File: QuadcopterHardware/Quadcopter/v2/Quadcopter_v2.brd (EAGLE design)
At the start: 47 x 28 mm, 43 parts, among them J1 FTDI_DEVICE, M1 WIRELESS-NRF24L01, U1 ATMEGA328P_TQFP, U3 GY-521MPU6050

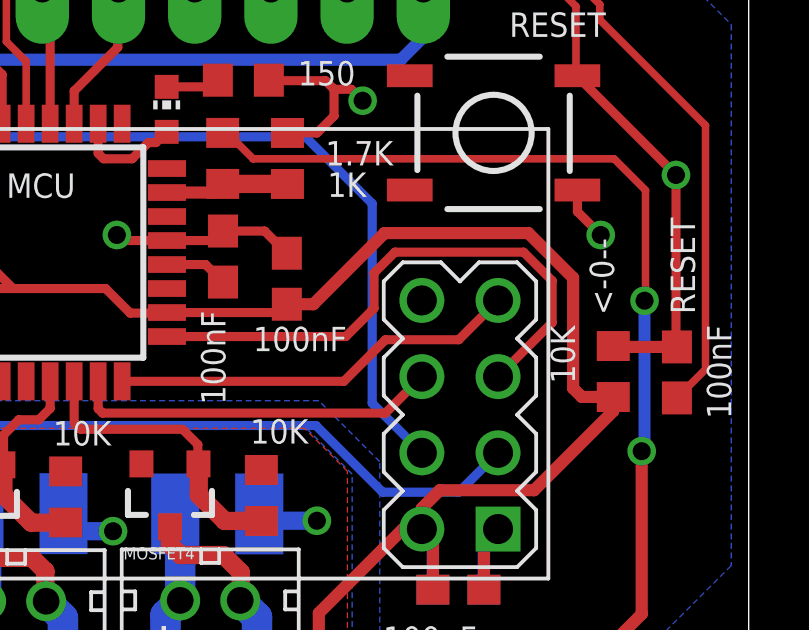
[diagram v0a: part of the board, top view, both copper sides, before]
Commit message: removed unnecessary trace
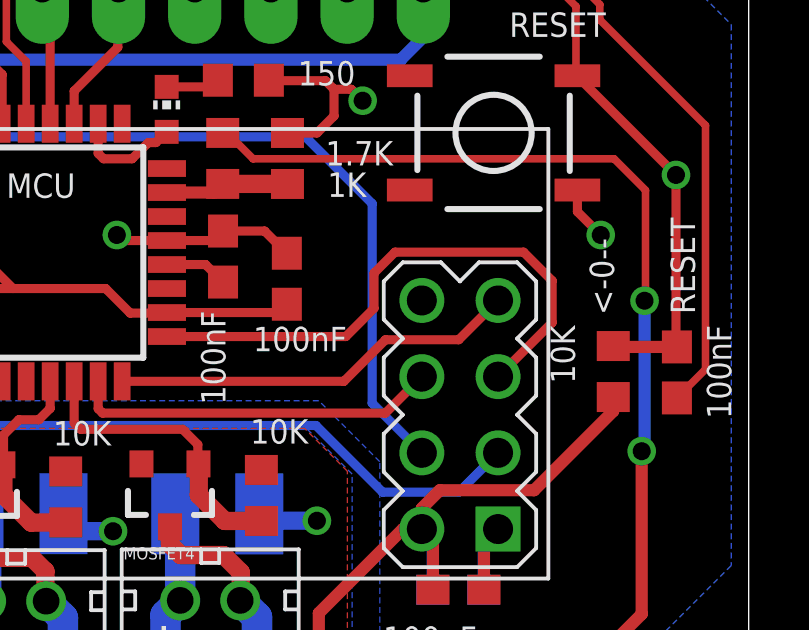
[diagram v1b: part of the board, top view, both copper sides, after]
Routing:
- net 3V3: track 146.4 -> 130.1 mm
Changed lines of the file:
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@@
 <wire x1="26.38425" y1="13.93825" x2="27.58985" y2="13.93825" width="0.3048" layer="1"/>
 <wire x1="27.58985" y1="13.93825" x2="27.60835" y2="13.95675" width="0.3048" layer="1"/>
-<wire x1="31.60575" y1="14.233" x2="32.48925" y2="14.233" width="0.4064" layer="1"/>
-<wire x1="32.48925" y1="14.233" x2="34.8615" y2="16.60525" width="0.4064" layer="1"/>
-<wire x1="34.8615" y1="16.60525" x2="39.65575" y2="16.60525" width="0.4064" layer="1"/>
-<wire x1="39.65575" y1="16.60525" x2="41.148" y2="15.113" width="0.4064" layer="1"/>
-<wire x1="41.148" y1="15.113" x2="41.148" y2="11.43" width="0.4064" layer="1"/>
-<wire x1="41.148" y1="11.43" x2="41.43375" y2="11.14425" width="0.4064" layer="1"/>
-<wire x1="41.43375" y1="11.14425" x2="42.482" y2="11.14425" width="0.4064" layer="1"/>
-<wire x1="42.482" y1="11.14425" x2="42.486" y2="11.14025" width="0.3048" layer="1"/>
 <wire x1="16.1185" y1="18.00025" x2="10.40825" y2="18.00025" width="0.3048" layer="1"/>
 <wire x1="10.40825" y1="18.00025" x2="9.5945" y2="17.1865" width="0.3048" layer="1"/>
